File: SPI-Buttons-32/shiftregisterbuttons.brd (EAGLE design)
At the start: 47 x 43 mm, 44 parts, among them IC1 74AC165D, IC2 74AC165D, IC3 74AC165D, IC4 74AC165D

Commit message: SPI button update
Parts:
- added C5: 100n, resistor:C0603
- added C6, C7: 4.7n, resistor:C0603
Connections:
- net CLK: now also C7.1
- net CS: now also C5.1
- net GND: now also C5.2, C6.2, C7.2
- net SER_OUT: now also C6.1
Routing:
- net SER_OUT: track 24.5 -> 26.2 mm
- net CLK: track 76.5 -> 77.7 mm
- net CS: track 71.4 -> 72.5 mm
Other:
- board text added: "YR 2022 V1.1 4x8b PISO shift registers w. pullups"
- board text removed: "YR 2022 V1.0 4x8b PISO shift registers w. pullups"

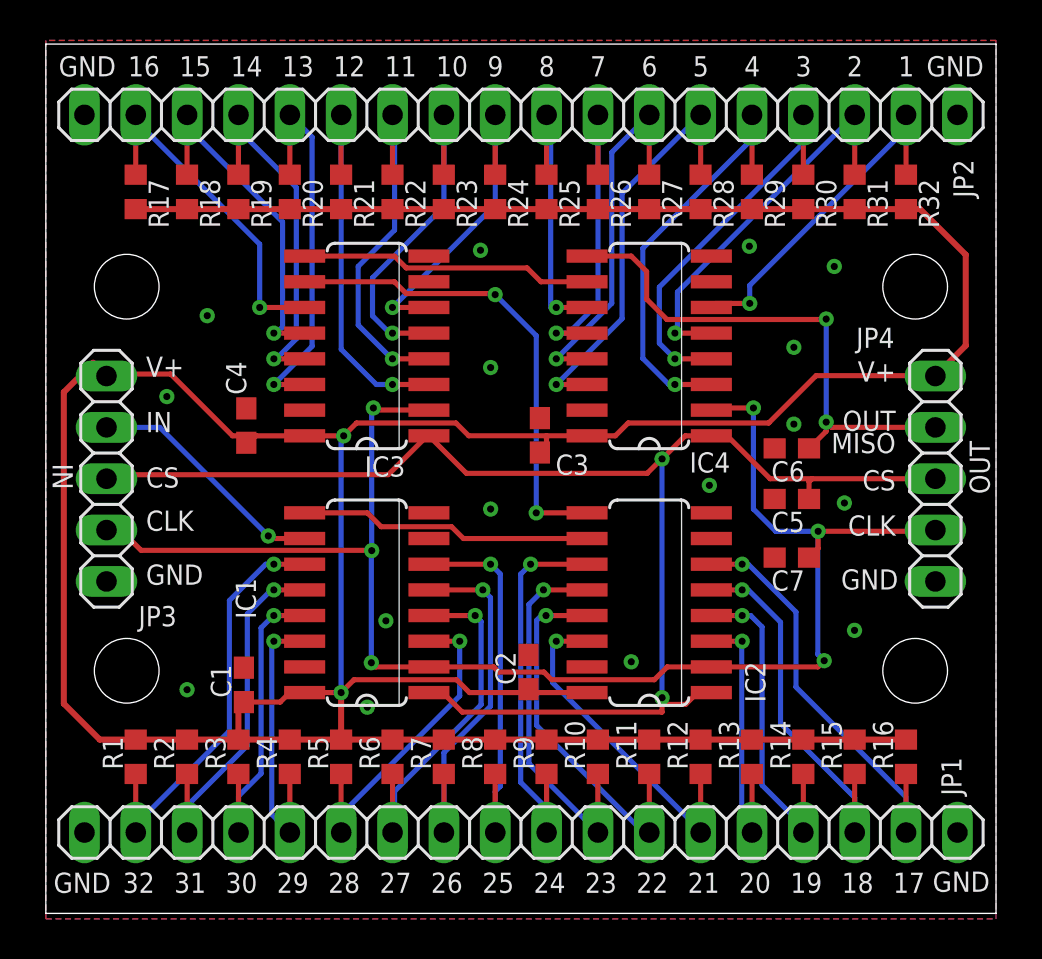
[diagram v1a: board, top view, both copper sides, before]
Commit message: Updated SPI buttons to v1.2
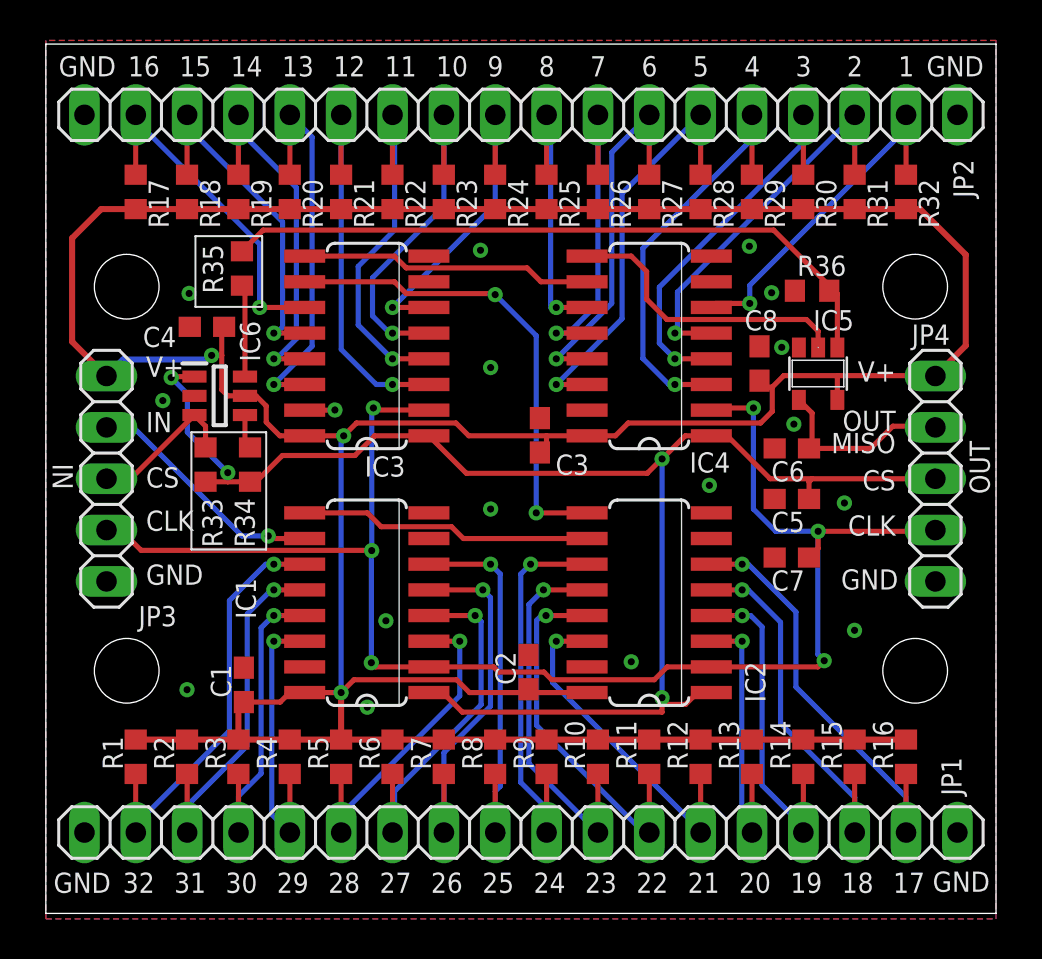
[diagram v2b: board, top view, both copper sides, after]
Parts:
- added C8: 1µ, resistor:C0603
- added IC5: 74LVC1G125DBV, 74xx-little-de:SOT23-5
- added IC6: SN74LVC2G14DBVRG4, SamacSys_Parts:SOT95P280X145-6N
- added R33, R34, R35: 0, resistor:R0603
- added R36: 10k, resistor:R0603
- moved C4 5.26 mm to (7.97, 29.0), turned to 180 degrees
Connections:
- new net CS_IN: IC6.3, JP3.3, R33.1
- new net NCS: IC6.4, R34.1
- new net NOE: IC6.6, R35.2
- new net OE_N: IC5.1, R35.1, R36.2
- new net SER_OUT_PREBUF: IC4.9, IC5.2
- net +3V3: now also C8.1, IC5.5, IC6.5
- net CS: now also IC6.1, R33.2, R34.2; no longer JP3.3
- net GND: now also C8.2, IC5.3, IC6.2, R36.1
- net SER_OUT: now also IC5.4; no longer IC4.9
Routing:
- net OE_N: track 0.00 -> 34.0 mm
- net SER_OUT: track 26.2 -> 9.46 mm, vias 2 -> 0
- net SER_OUT_PREBUF: track 0.00 -> 14.6 mm
- net CS_IN: track 0.00 -> 7.48 mm
- net +3V3: track 190.1 -> 184.7 mm, vias 2 -> 3
- net NOE: track 0.00 -> 4.56 mm
- net CS: track 72.5 -> 75.1 mm, vias 2 -> 4
- net NCS: track 0.00 -> 1.70 mm
- net GND: track 0.04 -> 1.55 mm, vias 16 -> 17
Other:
- board text added: "Jumpers: Connect R33 OR R34. R33: shift when CS HIGH (74xx165 mode) R34: shift when CS LOW (SPI mode) R35: enable tristate OUT/MOSI"
- board text added: "YR 2025 V1.2 4x8b PISO shift registers w. pullups"
- board text removed: "YR 2022 V1.1 4x8b PISO shift registers w. pullups"
